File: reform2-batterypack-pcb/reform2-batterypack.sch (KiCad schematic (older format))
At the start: 14 parts, among them J1 Conn_01x05_Female, U1 KEYSTONE_54, U2 KEYSTONE_54, U3 KEYSTONE_54, U4 KEYSTONE_54

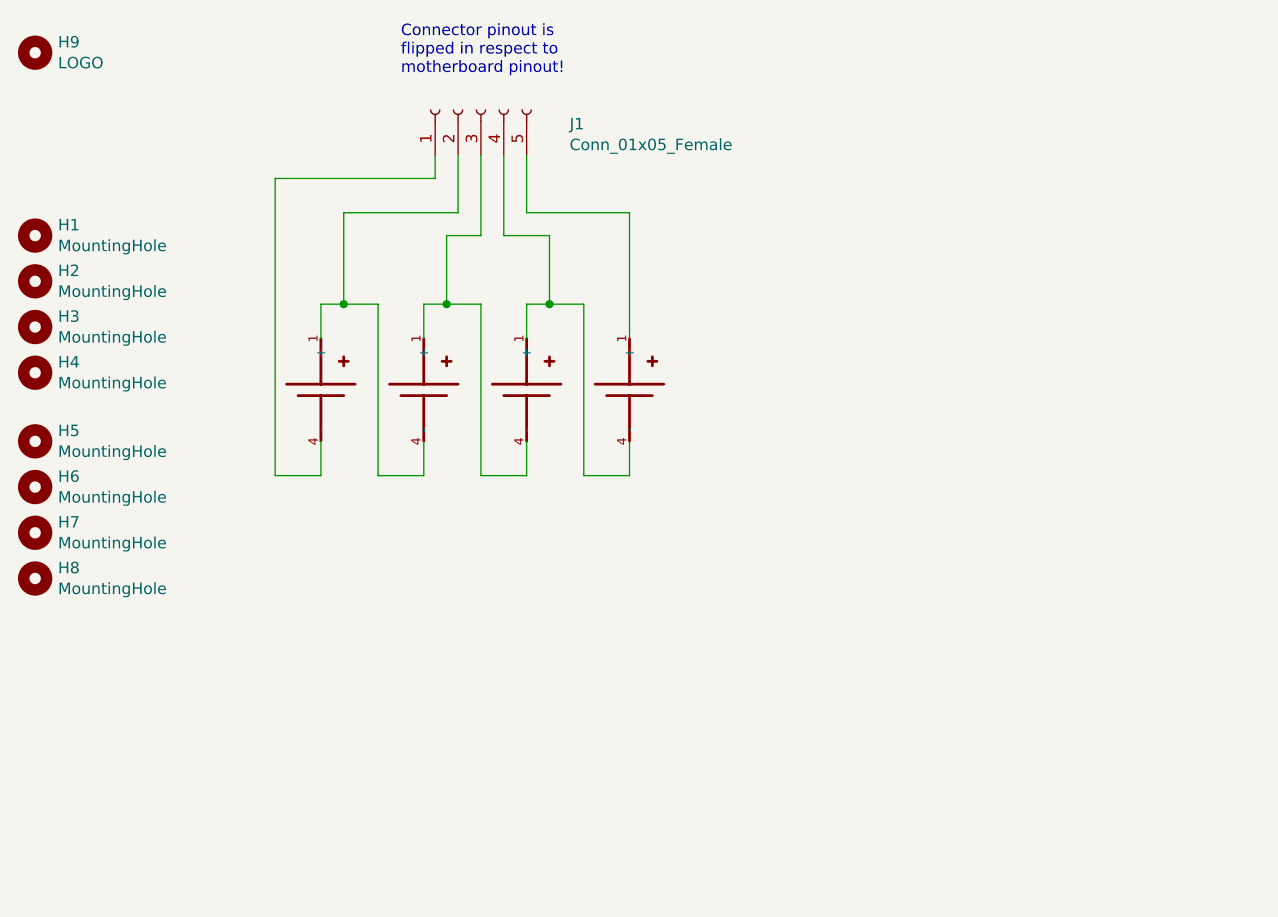
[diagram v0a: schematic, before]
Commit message: reform2: update PCBs incl. badges to production revs, add keyboard lettering, misc docs
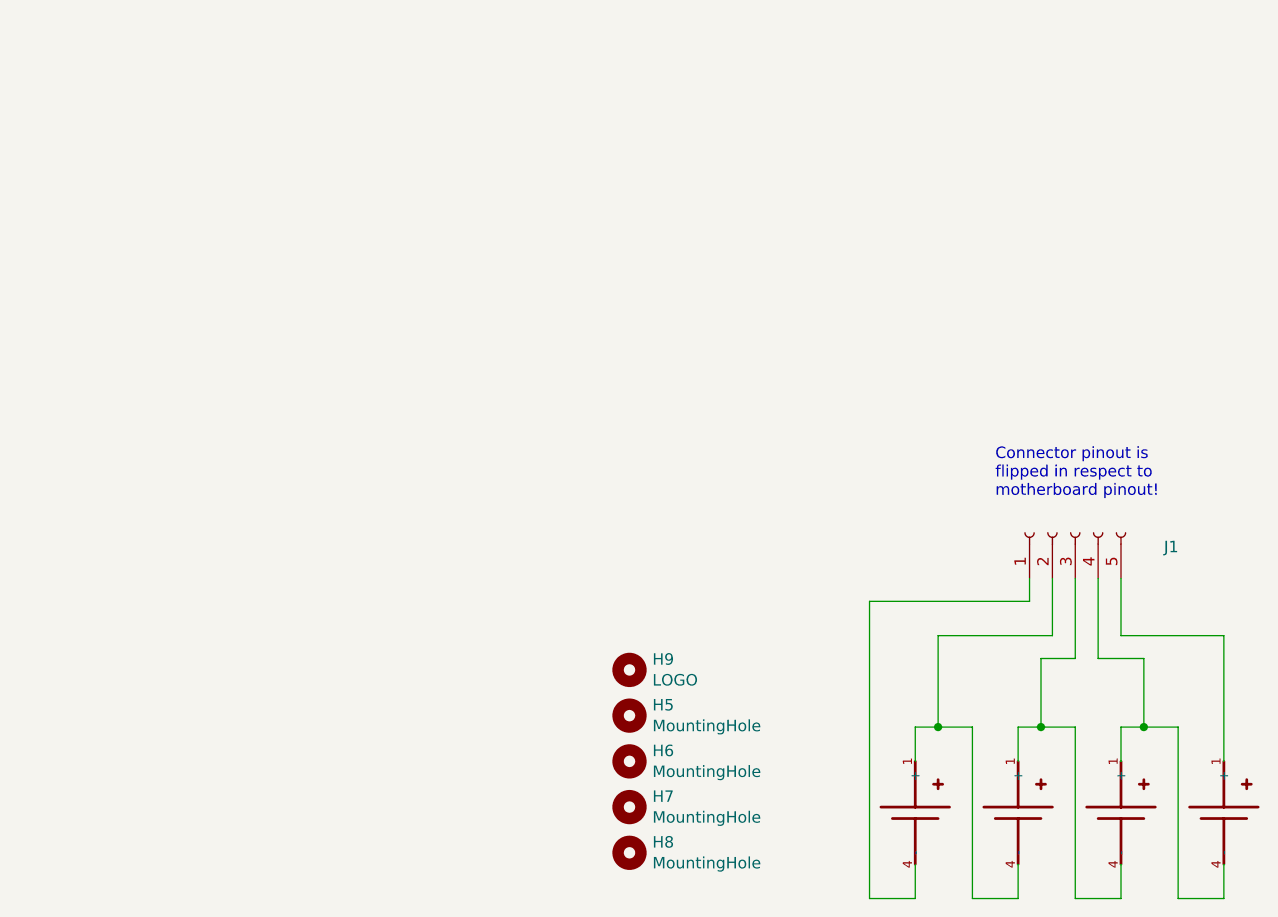
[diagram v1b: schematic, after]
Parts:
- removed H1, H2, H3, H4: MountingHole, MountingHole:MountingHole_2.2mm_M2, symbol Mechanical:MountingHole
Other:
- moved on the sheet: H5, H6, H7, H8, H9, J1
